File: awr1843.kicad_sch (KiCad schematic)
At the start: 2 parts, among them U3 AWR1843ABG_, U6 AWR1843ABG_

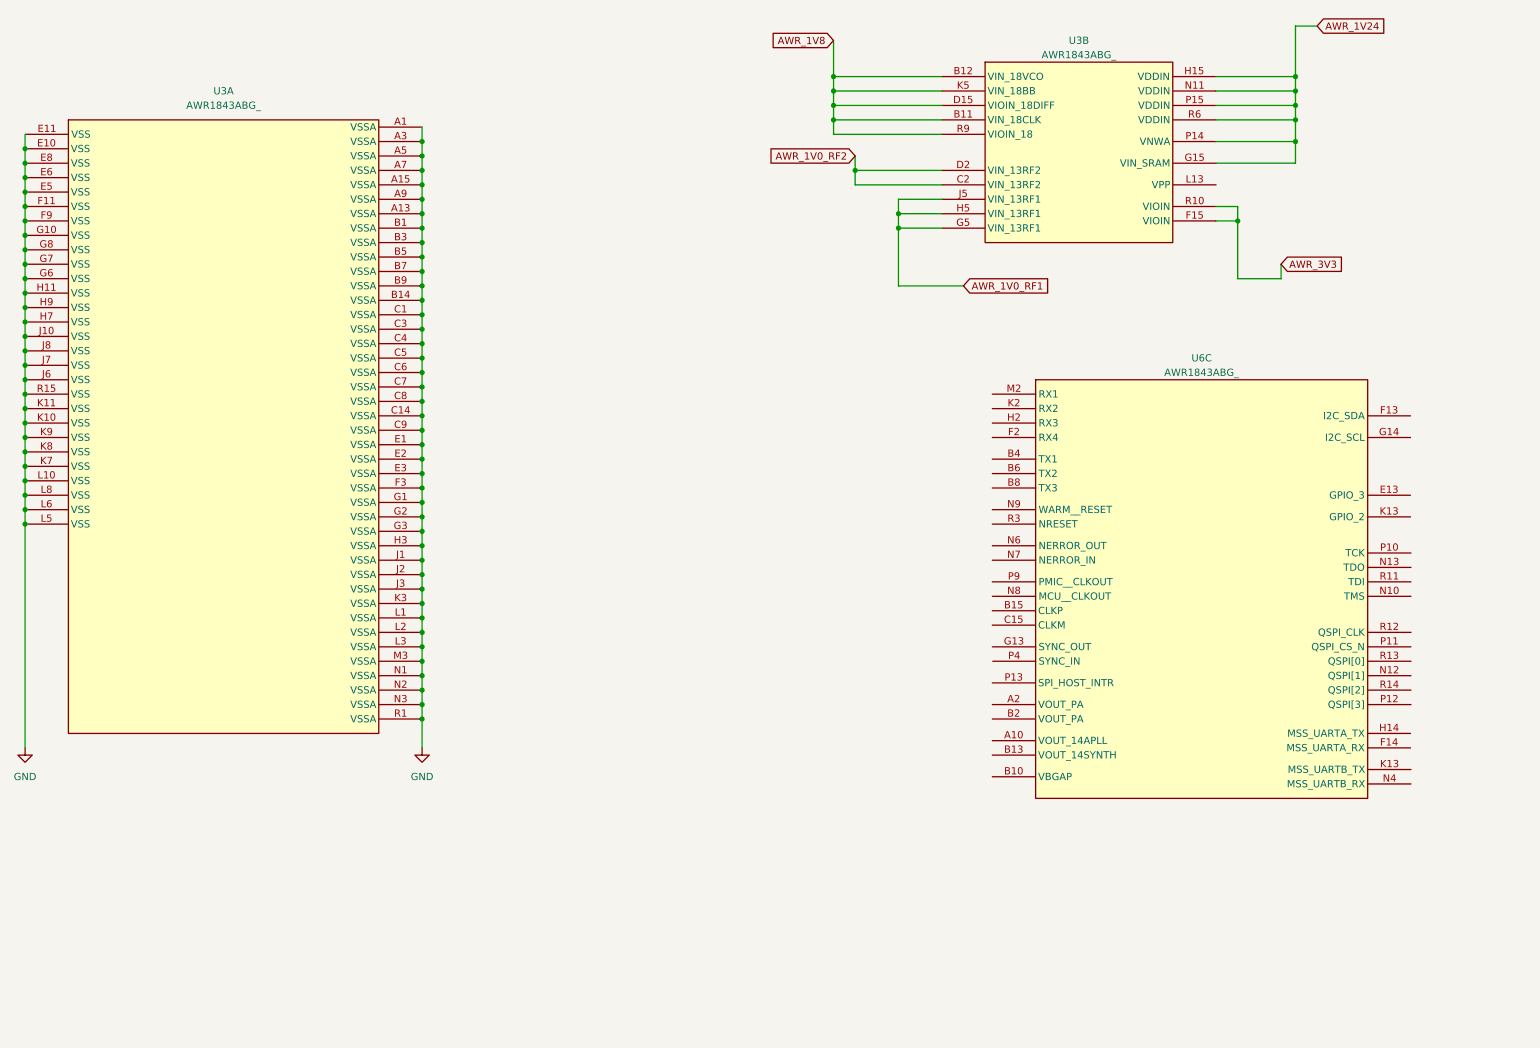
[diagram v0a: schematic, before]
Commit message: finding exact crystal used in ref design, finishing shcematics
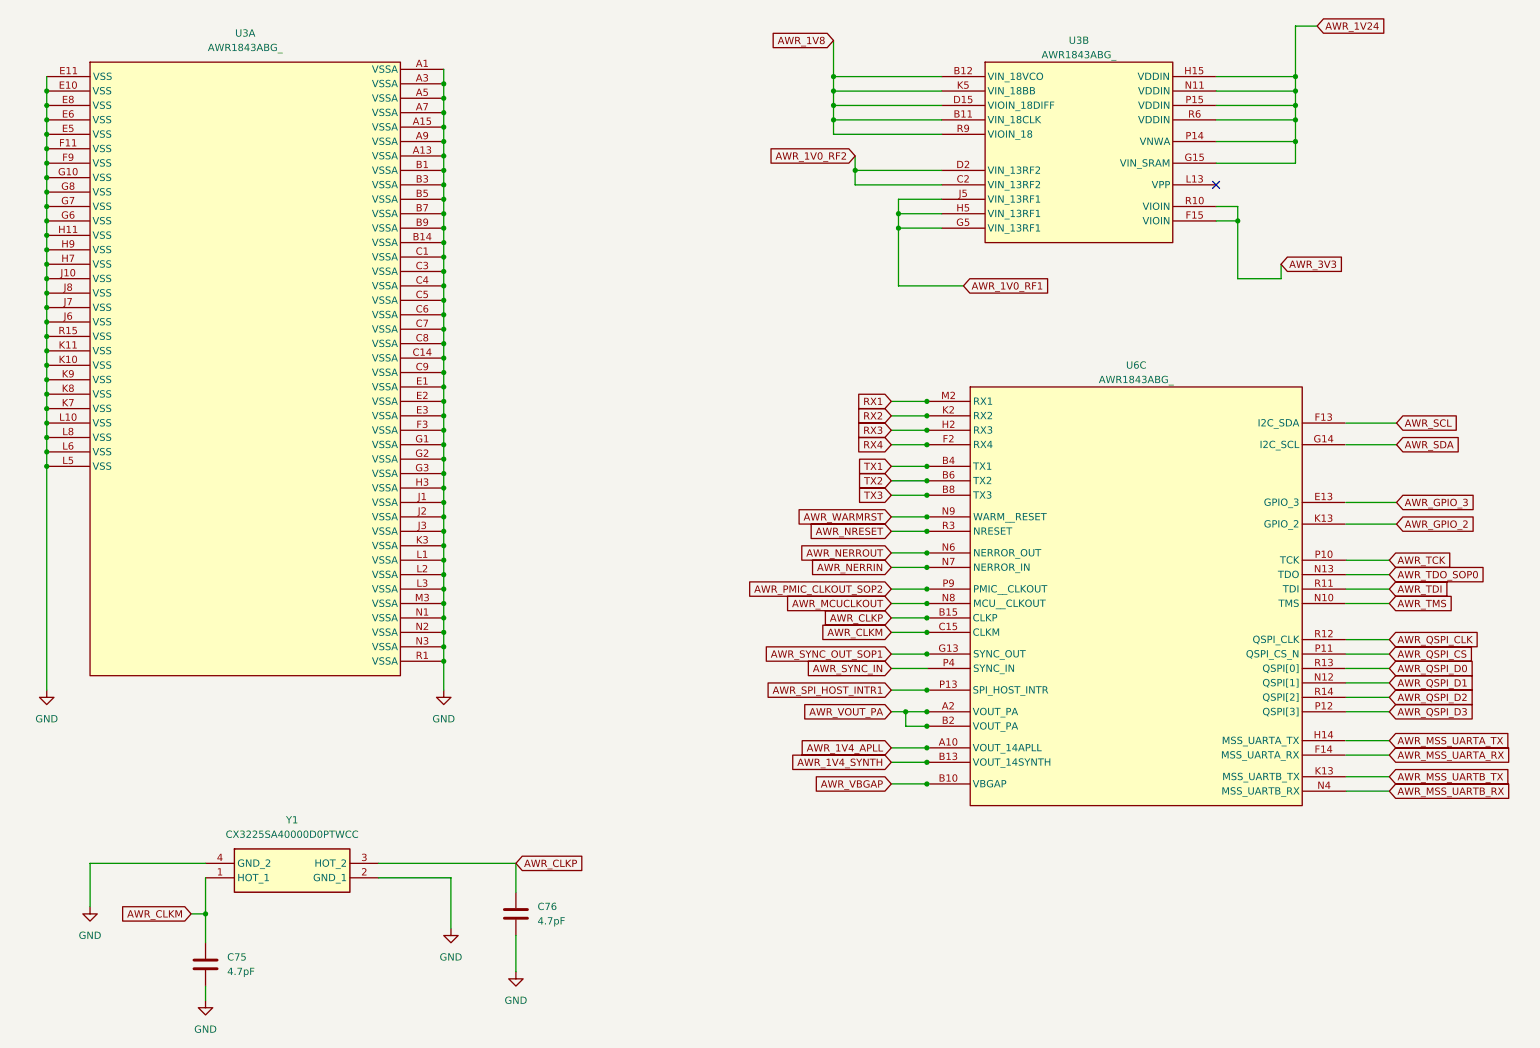
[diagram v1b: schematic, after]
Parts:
- added C75, C76: 4.7pF, symbol Device:C
- added Y1: CX3225SA40000D0PTWCC, CX3225SA40000D0PTWCC, symbol CX3225SA:CX3225SA40000D0PTWCC
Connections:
- net GND: now also C75.2, C76.2, Y1.2 (GND_1), Y1.4 (GND_2)
- net AWR_1V4_APLL: now reaches U6.A10 (VOUT_14APLL)
- net AWR_VOUT_PA: now reaches U6.A2 (VOUT_PA)
- net AWR_VOUT_PA: now also U6.B2 (VOUT_PA)
- net AWR_VBGAP: now reaches U6.B10 (VBGAP)
- net AWR_1V4_SYNTH: now reaches U6.B13 (VOUT_14SYNTH)
- net AWR_CLKP: now reaches U6.B15 (CLKP)
- net AWR_CLKP: now also C76.1, Y1.3 (HOT_2)
- net TX1: now reaches U6.B4 (TX1)
- net TX2: now reaches U6.B6 (TX2)
- net TX3: now reaches U6.B8 (TX3)
- net AWR_CLKM: now reaches U6.C15 (CLKM)
- net AWR_CLKM: now also C75.1, Y1.1 (HOT_1)
- net RX4: now reaches U6.F2 (RX4)
- net AWR_SYNC_OUT_SOP1: now reaches U6.G13 (SYNC_OUT)
- net RX3: now reaches U6.H2 (RX3)
- net RX2: now reaches U6.K2 (RX2)
- net RX1: now reaches U6.M2 (RX1)
- net AWR_NERROUT: now reaches U6.N6 (NERROR_OUT)
- net AWR_NERRIN: now reaches U6.N7 (NERROR_IN)
- net AWR_MCUCLKOUT: now reaches U6.N8 (MCU__CLKOUT)
- net AWR_WARMRST: now reaches U6.N9 (WARM__RESET)
- net AWR_SPI_HOST_INTR1: now reaches U6.P13 (SPI_HOST_INTR)
- net AWR_SYNC_IN: now reaches U6.P4 (SYNC_IN)
- net AWR_PMIC_CLKOUT_SOP2: now reaches U6.P9 (PMIC__CLKOUT)
- net AWR_NRESET: now reaches U6.R3 (NRESET)
- no-connect marks 0 -> 1
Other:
- moved on the sheet: U3A, U6C

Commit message: squashing ERC errors
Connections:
- net AWR_1V24: now also U3.H15 (VDDIN)
- net AWR_GPIO_2: now also U6.K13 (MSS_UARTB_TX)
- net AWR_GPIO_3: now also U6.E13 (GPIO_3)
- net AWR_MSS_UARTA_RX: now also U6.F14 (MSS_UARTA_RX)
- net AWR_MSS_UARTA_TX: now also U6.H14 (MSS_UARTA_TX)
- net AWR_MSS_UARTB_RX: now also U6.N4 (MSS_UARTB_RX)
- net AWR_MSS_UARTB_TX: now also U6.K13 (MSS_UARTB_TX)
- net AWR_QSPI_CLK: now also U6.R12 (QSPI_CLK)
- net AWR_QSPI_CS: now also U6.P11 (QSPI_CS_N)
- net AWR_QSPI_D0: now also U6.R13 (QSPI[0])
- net AWR_QSPI_D1: now also U6.N12 (QSPI[1])
- net AWR_QSPI_D2: now also U6.R14 (QSPI[2])
- net AWR_QSPI_D3: now also U6.P12 (QSPI[3])
- net AWR_SCL: now also U6.F13 (I2C_SDA)
- net AWR_SDA: now also U6.G14 (I2C_SCL)
- net AWR_TCK: now also U6.P10 (TCK)
- net AWR_TDI: now also U6.R11 (TDI)
- net AWR_TDO_SOP0: now also U6.N13 (TDO)
- net AWR_TMS: now also U6.N10 (TMS)
- net GND: now also U3.E11 (VSS)

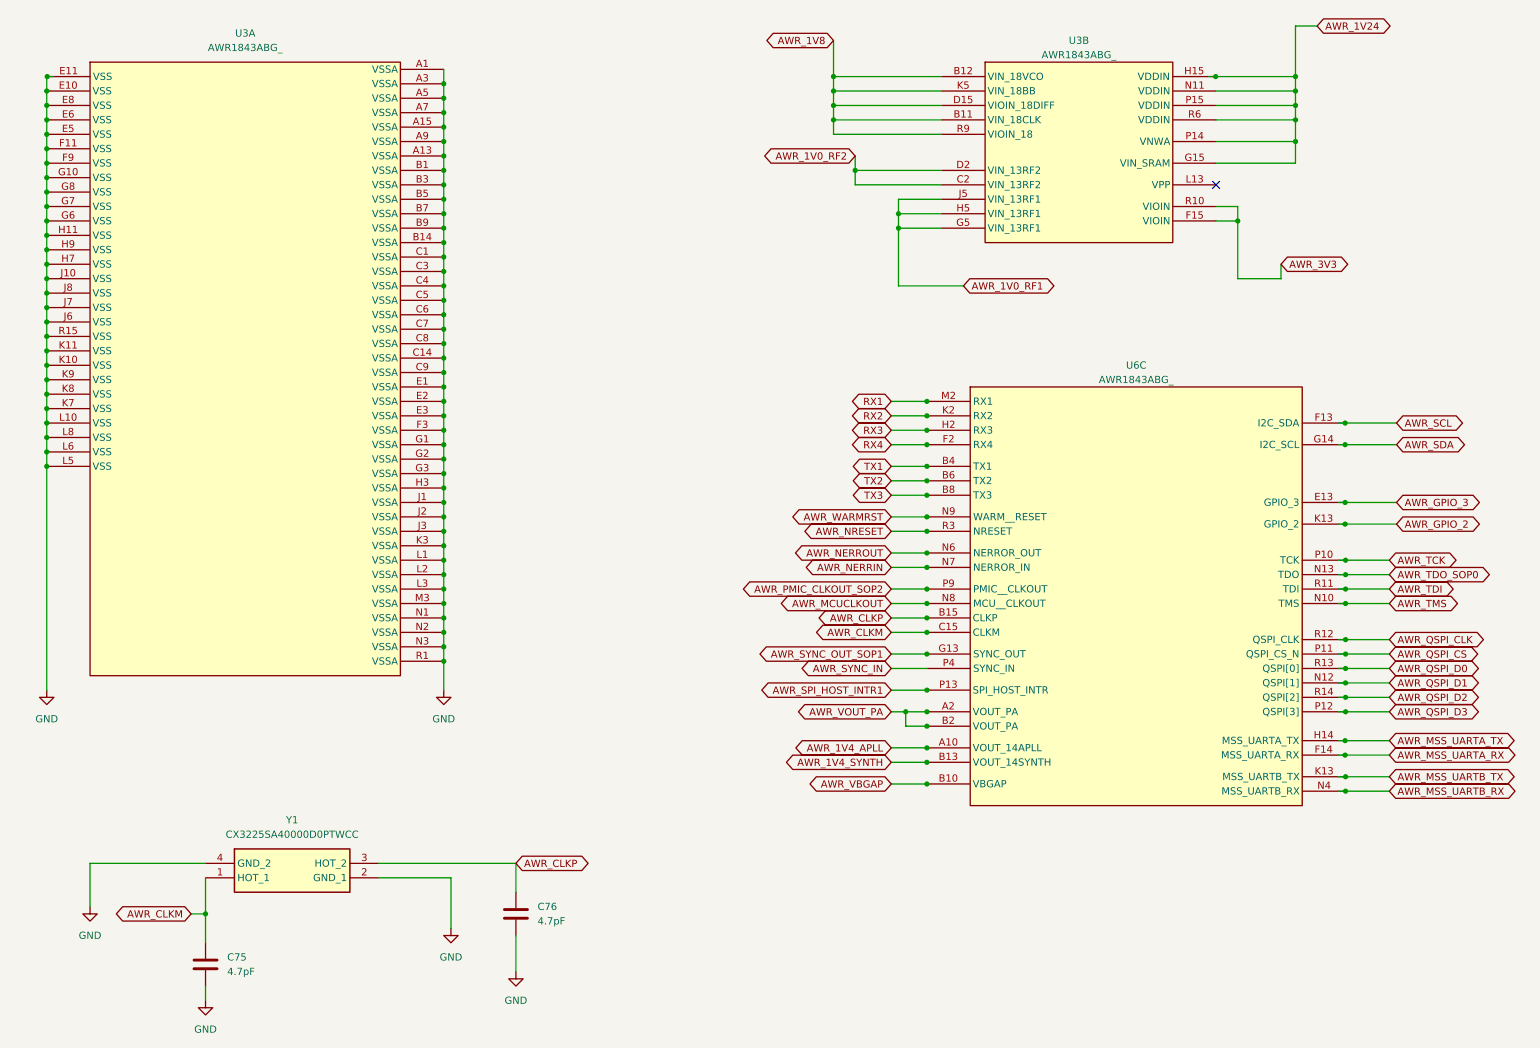
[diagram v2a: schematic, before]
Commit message: squashed ERC errors, moving onto pcb, grabbing fuse footprint
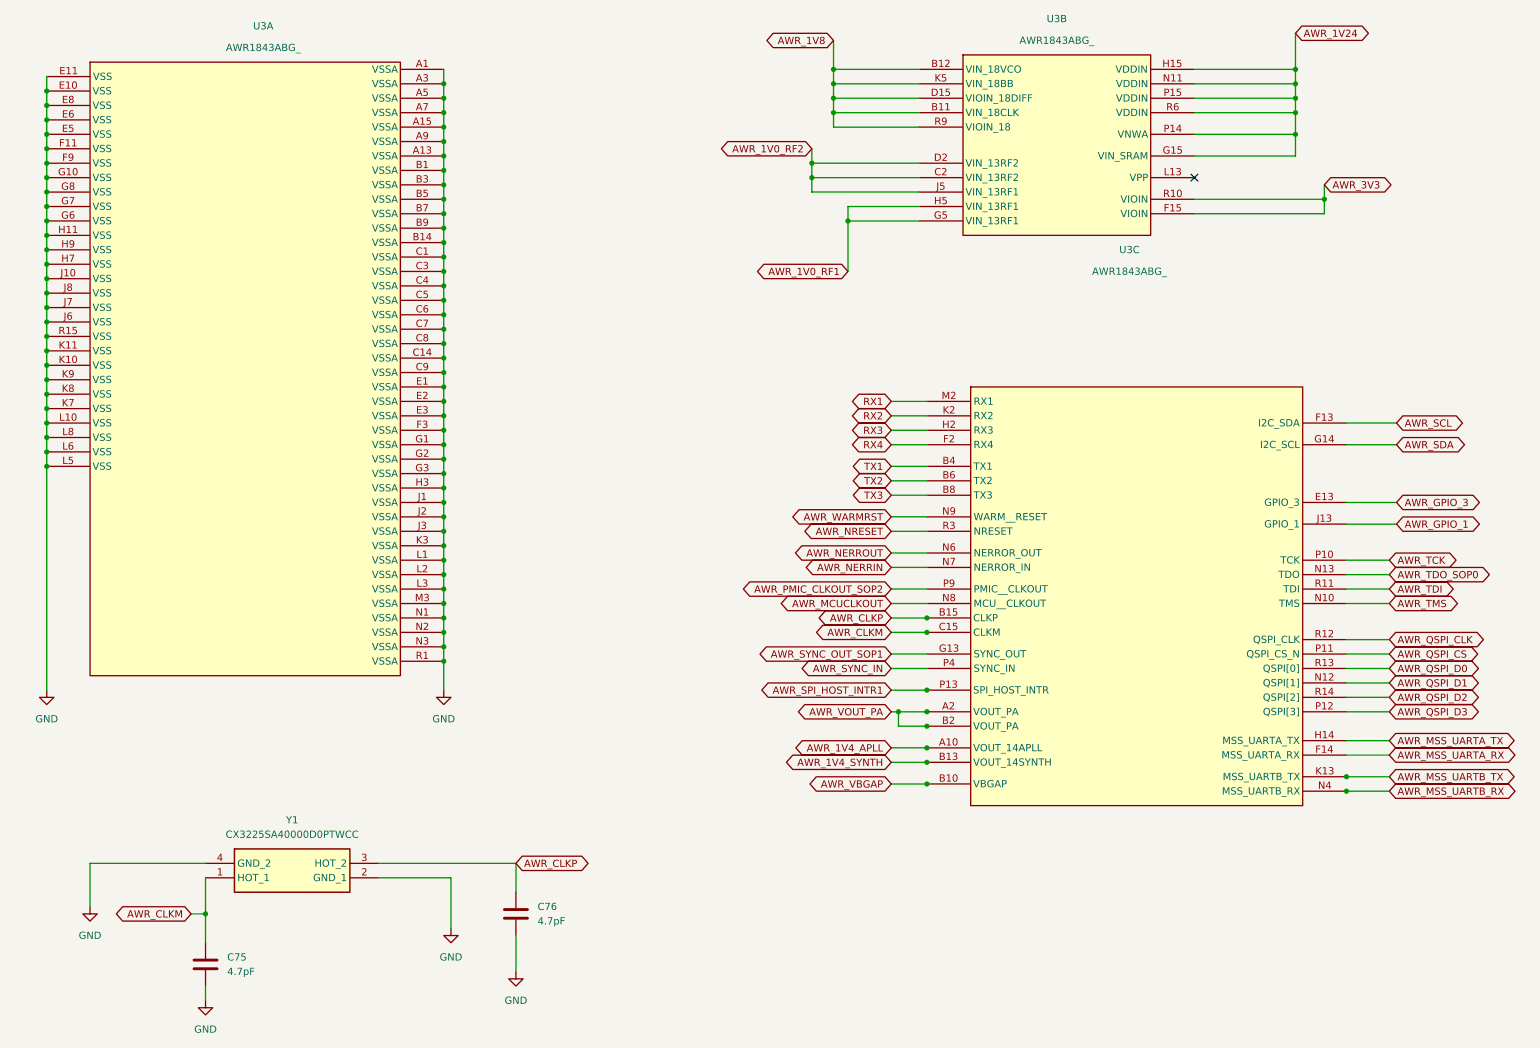
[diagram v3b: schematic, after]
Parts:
- removed U6: AWR1843ABG_, symbol AWR1843ABGABLRQ1:AWR1843ABG_
- added unit 3 of U3
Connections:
- net AWR_1V0_RF1: no longer U3.J5 (VIN_13RF1)
- net AWR_1V0_RF2: now also U3.J5 (VIN_13RF1)
- net AWR_1V24: no longer U3.H15 (VDDIN)
- net AWR_1V4_APLL: now also U3.A10 (VOUT_14APLL)
- net AWR_1V4_SYNTH: now also U3.B13 (VOUT_14SYNTH)
- net AWR_CLKM: now also U3.C15 (CLKM)
- net AWR_CLKP: now also U3.B15 (CLKP)
- net AWR_GPIO_3: now also U3.E13 (GPIO_3)
- net AWR_MCUCLKOUT: now also U3.N8 (MCU__CLKOUT)
- net AWR_MSS_UARTA_RX: now also U3.F14 (MSS_UARTA_RX)
- net AWR_MSS_UARTA_TX: now also U3.H14 (MSS_UARTA_TX)
- net AWR_MSS_UARTB_RX: now also U3.N4 (MSS_UARTB_RX)
- net AWR_MSS_UARTB_TX: now also U3.K13 (MSS_UARTB_TX)
- net AWR_NERRIN: now also U3.N7 (NERROR_IN)
- net AWR_NERROUT: now also U3.N6 (NERROR_OUT)
- net AWR_NRESET: now also U3.R3 (NRESET)
- net AWR_PMIC_CLKOUT_SOP2: now also U3.P9 (PMIC__CLKOUT)
- net AWR_QSPI_CLK: now also U3.R12 (QSPI_CLK)
- net AWR_QSPI_CS: now also U3.P11 (QSPI_CS_N)
- net AWR_QSPI_D0: now also U3.R13 (QSPI[0])
- net AWR_QSPI_D1: now also U3.N12 (QSPI[1])
- net AWR_QSPI_D2: now also U3.R14 (QSPI[2])
- net AWR_QSPI_D3: now also U3.P12 (QSPI[3])
- net AWR_SCL: now also U3.F13 (I2C_SDA)
- net AWR_SDA: now also U3.G14 (I2C_SCL)
- net AWR_SPI_HOST_INTR1: now also U3.P13 (SPI_HOST_INTR)
- net AWR_SYNC_IN: now also U3.P4 (SYNC_IN)
- net AWR_SYNC_OUT_SOP1: now also U3.G13 (SYNC_OUT)
- net AWR_TCK: now also U3.P10 (TCK)
- net AWR_TDI: now also U3.R11 (TDI)
- net AWR_TDO_SOP0: now also U3.N13 (TDO)
- net AWR_TMS: now also U3.N10 (TMS)
- net AWR_VBGAP: now also U3.B10 (VBGAP)
- net AWR_VOUT_PA: now also U3.A2 (VOUT_PA), U3.B2 (VOUT_PA)
- net AWR_WARMRST: now also U3.N9 (WARM__RESET)
- net RX1: now also U3.M2 (RX1)
- net RX2: now also U3.K2 (RX2)
- net RX3: now also U3.H2 (RX3)
- net RX4: now also U3.F2 (RX4)
- net TX1: now also U3.B4 (TX1)
- net TX2: now also U3.B6 (TX2)
- net TX3: now also U3.B8 (TX3)
- new net AWR_GPIO_1: U3.J13 (GPIO_1)
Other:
- moved on the sheet: U3B

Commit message: adding footprints
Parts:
- C75, C76: footprint (none) -> Capacitor_SMD:C_0603_1608Metric
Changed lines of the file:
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@@
       (effects (font (size 1.27 1.27)) (justify left))
     )
-    (property "Footprint" "" (at 50.4952 187.96 0)
+    (property "Footprint" "Capacitor_SMD:C_0603_1608Metric" (at 50.4952 187.96 0)
       (effects (font (size 1.27 1.27)) hide)
     )
@@
       (effects (font (size 1.27 1.27)) (justify left))
     )
-    (property "Footprint" "" (at 105.1052 179.07 0)
+    (property "Footprint" "Capacitor_SMD:C_0603_1608Metric" (at 105.1052 179.07 0)
       (effects (font (size 1.27 1.27)) hide)
     )
